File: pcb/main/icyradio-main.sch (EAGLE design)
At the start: 384 parts, among them CON301 FPC-40P, J701 TRSJACK, J702 TRSJACK, J703 TRSJACK, Q801 AO3400, Q802 AO3400, U1001 MIC23155, U1002 MIC23159, U1003 MIC2019, U1004 ADP150UJZ-1.8, U1005 ADP150UJZ-3.3, U1006 MIC94305, U1007 MIC94305, U101 EFM32GG11B420F2048GL112, U201 ATSAMV71Q21B-C, U301 ICE40HX8K-CT256, U302 SST26VF064B, U401 DSC1211DE3-C0017, U402 LTC2206, U403 R820T2, U501 ADL5385, U502 AD9117, U503 ADL5601, U601 DSC1201DE3-50M00000, U602 ADF4351, U701 TSCS25A3X1NDGXZAX, U702 CP2615, U801 ER-TFT035-6, U901 DSC1201DE3-50M00000, U902 SI5351C, X101 32.768 kHz, X401 DNP, X901 DNP

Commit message: Remove wrong LCSC item numbers
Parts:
- X401, X901: OCLCSC C70562 -> (none)
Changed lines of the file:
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@@
 <part name="GND420" library="Supply Symbol" deviceset="GND" device=""/>
 <part name="U401" library="Microchip" deviceset="DSC121*" device="" technology="1DE3-C0017"/>
-<part name="X401" library="Crystal" deviceset="CRYSTAL_4P" device="" value="DNP">
-<attribute name="OCLCSC" value="C70562"/>
-</part>
+<part name="X401" library="Crystal" deviceset="CRYSTAL_4P" device="" value="DNP"/>
 <part name="C412" library="Capacitor" deviceset="CAPACITOR" device="-0603" value="DNP"/>
 <part name="C410" library="Capacitor" deviceset="CAPACITOR" device="-0603" value="DNP"/>
@@
 <part name="GND902" library="Supply Symbol" deviceset="GND" device=""/>
 <part name="GND911" library="Supply Symbol" deviceset="GND" device=""/>
-<part name="X901" library="Crystal" deviceset="CRYSTAL_4P" device="" value="DNP">
-<attribute name="OCLCSC" value="C70562"/>
-</part>
+<part name="X901" library="Crystal" deviceset="CRYSTAL_4P" device="" value="DNP"/>
 <part name="C906" library="Capacitor" deviceset="CAPACITOR" device="-0603" value="DNP"/>
 <part name="C903" library="Capacitor" deviceset="CAPACITOR" device="-0603" value="DNP"/>
@@
 <attribute name="NAME" x="233.68" y="280.416" size="1.778" layer="95"/>
 <attribute name="VALUE" x="233.68" y="276.86" size="1.778" layer="96"/>
-<attribute name="OCLCSC" x="228.6" y="279.4" size="1.778" layer="96" display="off"/>
 </instance>
 <instance part="C412" gate="G$1" x="241.3" y="256.54" smashed="yes" rot="R270">
@@
 <attribute name="NAME" x="284.48" y="166.116" size="1.778" layer="95"/>
 <attribute name="VALUE" x="284.48" y="162.56" size="1.778" layer="96"/>
-<attribute name="OCLCSC" x="279.4" y="165.1" size="1.778" layer="96" display="off"/>
 </instance>
 <instance part="C906" gate="G$1" x="292.1" y="154.94" smashed="yes" rot="R270">

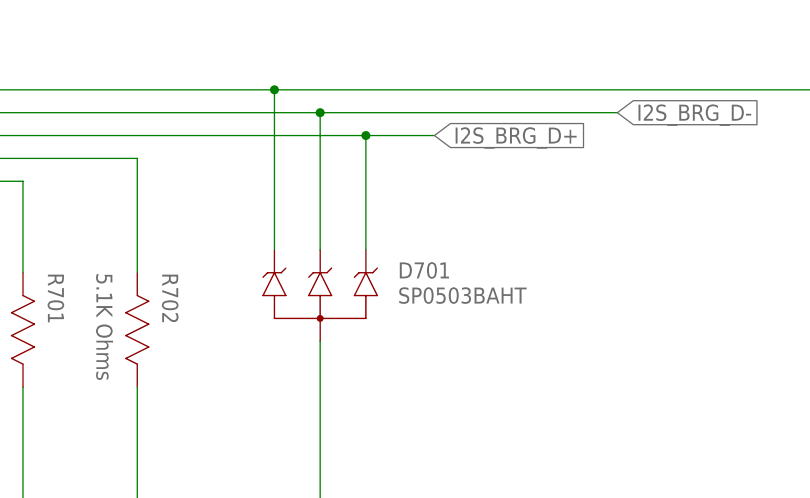
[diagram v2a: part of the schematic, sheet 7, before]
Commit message: Sync library updates on main PCB
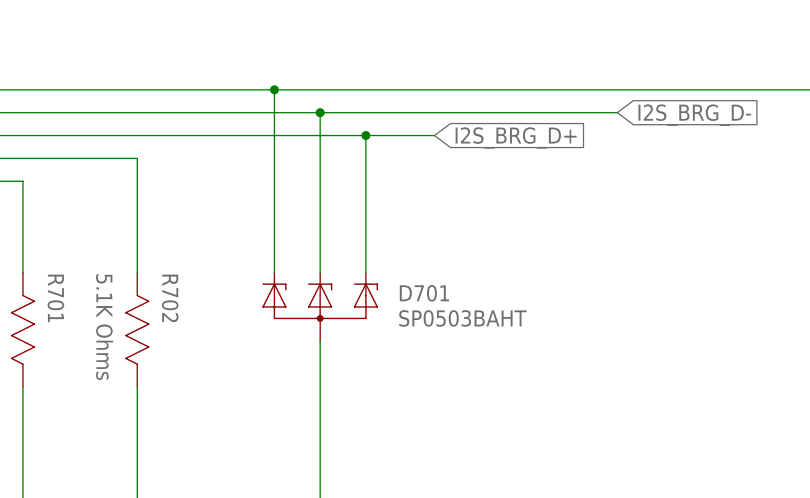
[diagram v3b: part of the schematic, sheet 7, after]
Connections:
- net DSP_D+: now also D1001.C3; no longer D1001.4
- net DSP_D-: now also D1001.C2; no longer D1001.3
- net GND: now also D1001.A, D701.A; no longer D1001.1, D701.1
- net I2S_BRG_D+: now also D701.C3; no longer D701.4
- net I2S_BRG_D-: now also D701.C2; no longer D701.3
- net I2S_BRG_VBUS: now also D701.C1; no longer D701.2
- net N$93: now also D1001.C1; no longer D1001.2
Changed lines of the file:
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@@
 <?xml version="1.0" encoding="utf-8"?>
 <!DOCTYPE eagle SYSTEM "eagle.dtd">
-<eagle version="9.5.2">
+<eagle version="9.5.1">
 <drawing>
 <settings>
@@
 </instance>
 <instance part="D701" gate="G$1" x="101.6" y="325.12" smashed="yes">
-<attribute name="NAME" x="110.236" y="329.565" size="1.778" layer="95"/>
-<attribute name="VALUE" x="110.236" y="326.771" size="1.778" layer="96"/>
+<attribute name="NAME" x="110.236" y="327.025" size="1.778" layer="95"/>
+<attribute name="VALUE" x="110.236" y="324.231" size="1.778" layer="96"/>
 </instance>
 <instance part="GND704" gate="G$1" x="101.6" y="304.8" smashed="yes">
@@
 <segment>
 <pinref part="GND704" gate="G$1" pin="GND"/>
-<pinref part="D701" gate="G$1" pin="1"/>
+<pinref part="D701" gate="G$1" pin="A"/>
 <wire x1="101.6" y1="304.8" x2="101.6" y2="322.58" width="0.1524" layer="91"/>
 </segment>
@@
 <net name="I2S_BRG_D-" class="0">
 <segment>
-<pinref part="D701" gate="G$1" pin="3"/>
+<pinref part="D701" gate="G$1" pin="C2"/>
 <pinref part="USB701" gate="G$1" pin="D-"/>
-<wire x1="101.6" y1="332.74" x2="101.6" y2="347.98" width="0.1524" layer="91"/>
 <wire x1="101.6" y1="347.98" x2="50.8" y2="347.98" width="0.1524" layer="91"/>
+<label x="134.62" y="347.98" size="1.778" layer="95" xref="yes"/>
 <wire x1="101.6" y1="347.98" x2="134.62" y2="347.98" width="0.1524" layer="91"/>
+<wire x1="101.6" y1="330.2" x2="101.6" y2="347.98" width="0.1524" layer="91"/>
 <junction x="101.6" y="347.98"/>
-<label x="134.62" y="347.98" size="1.778" layer="95" xref="yes"/>
 </segment>
 <segment>
@@
 <net name="I2S_BRG_VBUS" class="0">
 <segment>
-<pinref part="D701" gate="G$1" pin="2"/>
+<pinref part="D701" gate="G$1" pin="C1"/>
 <pinref part="USB701" gate="G$1" pin="VBUS"/>
-<wire x1="96.52" y1="332.74" x2="96.52" y2="350.52" width="0.1524" layer="91"/>
 <wire x1="96.52" y1="350.52" x2="50.8" y2="350.52" width="0.1524" layer="91"/>
 <pinref part="R705" gate="G$1" pin="2"/>
 <wire x1="187.96" y1="345.44" x2="187.96" y2="350.52" width="0.1524" layer="91"/>
-<wire x1="96.52" y1="350.52" x2="162.56" y2="350.52" width="0.1524" layer="91"/>
-<junction x="96.52" y="350.52"/>
 <pinref part="C706" gate="G$1" pin="C1"/>
+<wire x1="96.52" y1="350.52" x2="162.56" y2="350.52" width="0.1524" layer="91"/>
 <wire x1="162.56" y1="350.52" x2="175.26" y2="350.52" width="0.1524" layer="91"/>
 <wire x1="175.26" y1="350.52" x2="187.96" y2="350.52" width="0.1524" layer="91"/>
@@
 <wire x1="162.56" y1="345.44" x2="162.56" y2="350.52" width="0.1524" layer="91"/>
 <junction x="162.56" y="350.52"/>
+<wire x1="96.52" y1="330.2" x2="96.52" y2="350.52" width="0.1524" layer="91"/>
+<junction x="96.52" y="350.52"/>
 </segment>
 </net>
@@
 </segment>
 <segment>
-<pinref part="D701" gate="G$1" pin="4"/>
+<pinref part="D701" gate="G$1" pin="C3"/>
 <pinref part="USB701" gate="G$1" pin="D+"/>
-<wire x1="106.68" y1="332.74" x2="106.68" y2="345.44" width="0.1524" layer="91"/>
 <wire x1="106.68" y1="345.44" x2="50.8" y2="345.44" width="0.1524" layer="91"/>
+<label x="114.3" y="345.44" size="1.778" layer="95" xref="yes"/>
 <wire x1="106.68" y1="345.44" x2="114.3" y2="345.44" width="0.1524" layer="91"/>
+<wire x1="106.68" y1="330.2" x2="106.68" y2="345.44" width="0.1524" layer="91"/>
 <junction x="106.68" y="345.44"/>
-<label x="114.3" y="345.44" size="1.778" layer="95" xref="yes"/>
 </segment>
 </net>
@@
 </instance>
 <instance part="D1001" gate="G$1" x="104.14" y="317.5" smashed="yes">
-<attribute name="NAME" x="112.776" y="321.945" size="1.778" layer="95"/>
-<attribute name="VALUE" x="112.776" y="319.151" size="1.778" layer="96"/>
+<attribute name="NAME" x="112.776" y="319.405" size="1.778" layer="95"/>
+<attribute name="VALUE" x="112.776" y="316.611" size="1.778" layer="96"/>
 </instance>
 <instance part="GND1013" gate="G$1" x="104.14" y="297.18" smashed="yes">
@@
 <segment>
 <pinref part="GND1013" gate="G$1" pin="GND"/>
-<pinref part="D1001" gate="G$1" pin="1"/>
+<pinref part="D1001" gate="G$1" pin="A"/>
 <wire x1="104.14" y1="297.18" x2="104.14" y2="314.96" width="0.1524" layer="91"/>
 </segment>
@@
 <net name="DSP_D-" class="0">
 <segment>
-<pinref part="D1001" gate="G$1" pin="3"/>
-<wire x1="104.14" y1="325.12" x2="104.14" y2="340.36" width="0.1524" layer="91"/>
+<pinref part="D1001" gate="G$1" pin="C2"/>
 <wire x1="104.14" y1="340.36" x2="53.34" y2="340.36" width="0.1524" layer="91"/>
-<wire x1="104.14" y1="340.36" x2="137.16" y2="340.36" width="0.1524" layer="91"/>
-<junction x="104.14" y="340.36"/>
 <label x="137.16" y="340.36" size="1.778" layer="95" xref="yes"/>
 <pinref part="USB1001" gate="G$1" pin="D-"/>
+<wire x1="104.14" y1="340.36" x2="137.16" y2="340.36" width="0.1524" layer="91"/>
+<wire x1="104.14" y1="322.58" x2="104.14" y2="340.36" width="0.1524" layer="91"/>
+<junction x="104.14" y="340.36"/>
 </segment>
 </net>
 <net name="DSP_D+" class="0">
 <segment>
-<pinref part="D1001" gate="G$1" pin="4"/>
-<wire x1="109.22" y1="325.12" x2="109.22" y2="337.82" width="0.1524" layer="91"/>
+<pinref part="D1001" gate="G$1" pin="C3"/>
 <wire x1="109.22" y1="337.82" x2="53.34" y2="337.82" width="0.1524" layer="91"/>
-<wire x1="109.22" y1="337.82" x2="116.84" y2="337.82" width="0.1524" layer="91"/>
-<junction x="109.22" y="337.82"/>
 <label x="116.84" y="337.82" size="1.778" layer="95" xref="yes"/>
 <pinref part="USB1001" gate="G$1" pin="D+"/>
+<wire x1="109.22" y1="337.82" x2="116.84" y2="337.82" width="0.1524" layer="91"/>
+<wire x1="109.22" y1="322.58" x2="109.22" y2="337.82" width="0.1524" layer="91"/>
+<junction x="109.22" y="337.82"/>
 </segment>
 </net>
@@
 <net name="N$93" class="0">
 <segment>
-<pinref part="D1001" gate="G$1" pin="2"/>
-<wire x1="99.06" y1="325.12" x2="99.06" y2="350.52" width="0.1524" layer="91"/>
+<pinref part="D1001" gate="G$1" pin="C1"/>
 <pinref part="F1001" gate="G$1" pin="1"/>
 <wire x1="81.28" y1="350.52" x2="99.06" y2="350.52" width="0.1524" layer="91"/>
@@
 <wire x1="160.02" y1="327.66" x2="160.02" y2="350.52" width="0.1524" layer="91"/>
 <wire x1="160.02" y1="350.52" x2="99.06" y2="350.52" width="0.1524" layer="91"/>
-<junction x="99.06" y="350.52"/>
 <pinref part="L1003" gate="G$1" pin="1"/>
 <wire x1="167.64" y1="350.52" x2="160.02" y2="350.52" width="0.1524" layer="91"/>
 <junction x="160.02" y="350.52"/>
+<wire x1="99.06" y1="322.58" x2="99.06" y2="350.52" width="0.1524" layer="91"/>
+<junction x="99.06" y="350.52"/>
 </segment>
 </net>

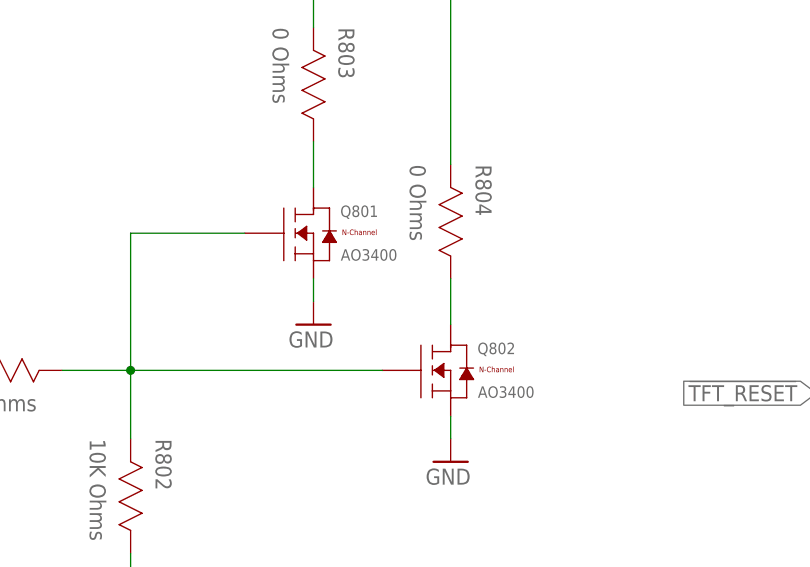
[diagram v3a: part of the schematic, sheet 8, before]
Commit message: Fix TRS Jack name on tPlace
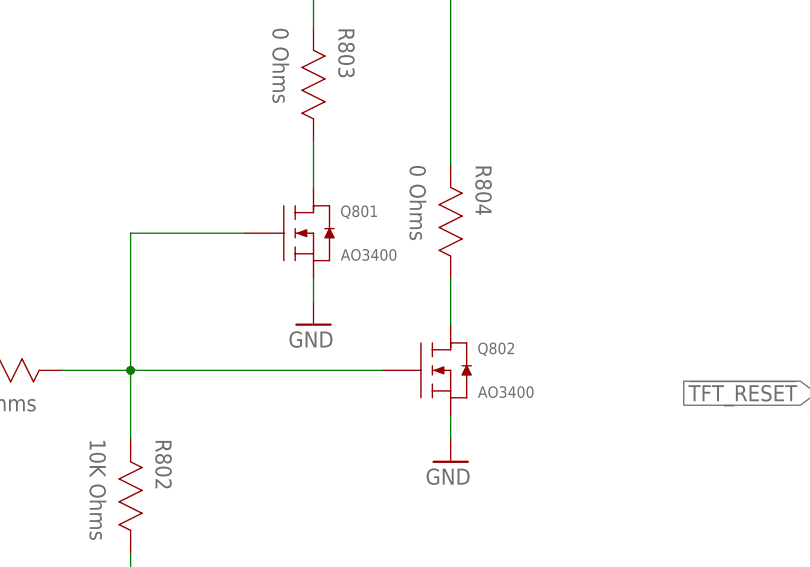
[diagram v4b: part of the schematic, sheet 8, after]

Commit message: Change wrong RGB LED package Change wrong DSC12x package Add extra 100nF capacitor Add extra 10K pullup on FPGA_CDONE Update schematic PDF Update board images Work on software Work on HDL
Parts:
- added C908: 100nF, Capacitor:CAPACITOR-0603
- added R306: 10K Ohms, Resistor:RESISTOR-0603
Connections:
- net 3V3: now also C908.C1, R306.2
- net FPGA_CDONE: now also R306.1
- net GND: now also C908.C2
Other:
- moved on the sheet: C301, C302, C303, C304, C305, C306, C307, C308, C309, C310, C311, C312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

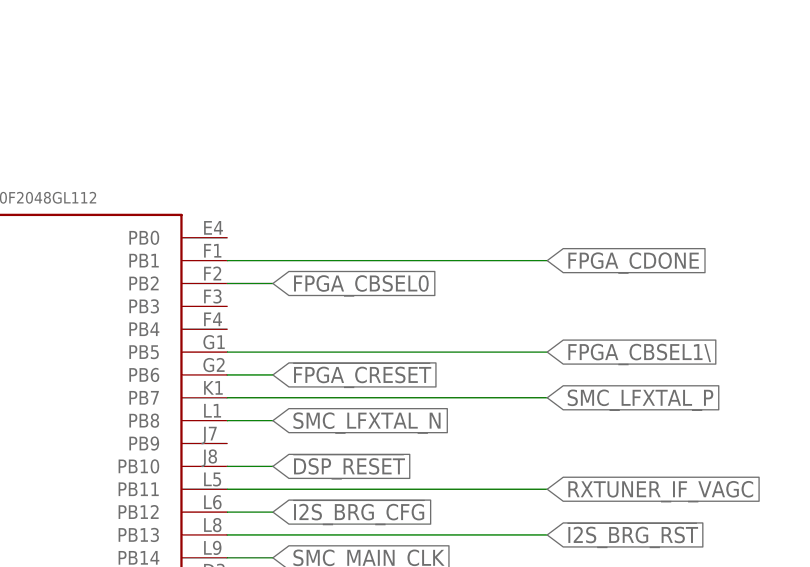
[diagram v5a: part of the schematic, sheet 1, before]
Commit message: Change FPGA_CBSEL0 signal name to FPGA_SMC_IRQ Added AD9117 library Extensively tested (lol) R820T2 library Added ARM CMSIS DSP functions to compute FFT in the SMC Small changes to the Verilog design Finally removed TFT bloat code Changed FPGA SPI from mode 3 to mode 0
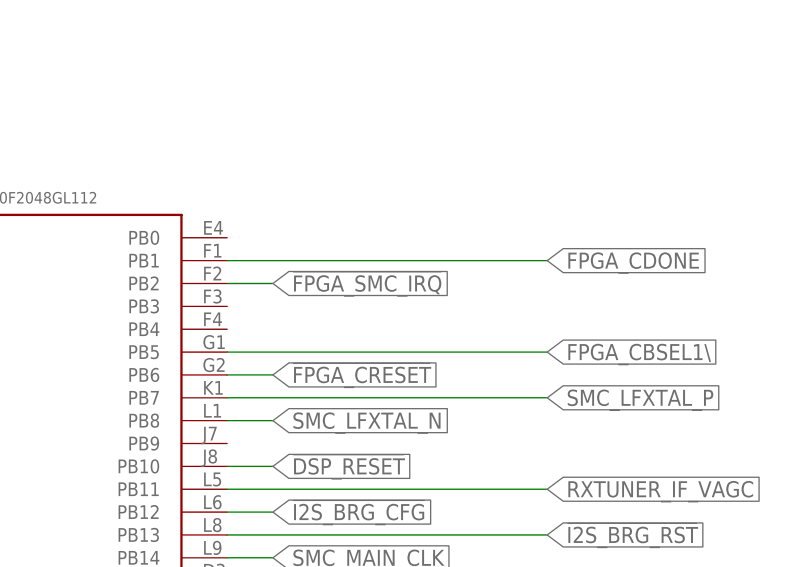
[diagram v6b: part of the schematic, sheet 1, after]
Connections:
- net FPGA_CBSEL0 renamed !FPGA_SMC_IRQ
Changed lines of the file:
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@@
 </segment>
 </net>
-<net name="FPGA_CBSEL0" class="0">
+<net name="!FPGA_SMC_IRQ" class="0">
 <segment>
 <wire x1="292.1" y1="297.18" x2="297.18" y2="297.18" width="0.1524" layer="91"/>
@@
 </segment>
 </net>
-<net name="FPGA_CBSEL0" class="0">
+<net name="!FPGA_SMC_IRQ" class="0">
 <segment>
 <pinref part="U301" gate=".BANK2SPI" pin="CBSEL0/IOB_103"/>
